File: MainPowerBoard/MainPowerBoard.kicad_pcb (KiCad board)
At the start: 2 copper layers, 177.8 x 177.8 mm, 243 parts, among them J101 CONN_01X04, J102 CONN_01X04, J103 CONN_01X04, J104 CONN_01X02, J105 CONN_01X02, J106 CONN_01X04, J107 CONN_01X06, J108 CONN_01X04, J109 CONN_01X04, J110 CONN_01X02, J111 CONN_01X02, J112 CONN_01X02, J113 CONN_01X02, J114 CONN_01X02, J115 CONN_01X02, J116 CONN_01X02, J117 CONN_01X02, J118 CONN_01X02, J119 CONN_01X02, J120 CONN_01X02, J121 CONN_01X02, J122 CONN_01X02, J123 CONN_01X02, J124 CONN_01X02, J125 CONN_01X02, J126 CONN_01X02, J127 CONN_01X02, J128 CONN_01X02, J129 CONN_01X02, J130 MOUNTING_HOLE, J131 MOUNTING_HOLE, J132 MOUNTING_HOLE, J133 MOUNTING_HOLE, SW701 GPTS203211B, U1001 LMR16030S, U1101 LMR16030S, U1201 LMR16030S, U1301 LMR16030S, U1401 LMR16030S, U201 LMR16030S, U301 LMR16030S, U701 ZXTR2012Z-7, U702 TLV271IDBVR, U703 LTC2950-1, U704 TLC393, U801 LMR16030S, U901 LMR16030S

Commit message: Done with layout - ready for final review before fab.
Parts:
- added G***: LOGO, hyperCustom:ParadigmLogo, F.Cu at (88.9, 88.9)
- D1004, D1104, D1204, D1304, D1404, D204, D804, D904: value 30V -> 28V
- D303: value 6V -> 7.5V
- D402, D502, D602: footprint Diodes_SMD:SOD-123 -> hyperCustom:SOD-123
- D501: footprint DD-PAK_TO263_SingleDiode_ThermalVias -> hyperCustom:DD-PAK_TO263_SingleDiode_ThermalVias
- J101, J102, J103, J106, J108, J109: footprint hyperCustom:CONN_PHOENIX_1844236_4PIN -> hyperCustom:CONN_PHOENIX_1844236_4PIN_1
- R1004, R1104, R1204, R1304, R1404, R204, R804, R904: value R -> 400
- R304: value R -> 300; footprint Resistors_SMD:R_1206_HandSoldering -> SMD_Packages:SMD-1206_Pol
- R401, R501, R601: value R -> 1.5k
- R703: value 10k -> 500k
- R705, R709: value R -> 300
- U701: value ZXTR2012Z-7 -> UA78L05CPK
- moved D403 5.78 mm to (20.8, 116.1), turned to 180 degrees
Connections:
- C702 pad 1: /On-Off Switch/12V0 -> /On-Off Switch/5V0
- D701 pad 2: /On-Off Switch/12V0 -> /On-Off Switch/5V0
- D702 pad 2: /On-Off Switch/12V0 -> /On-Off Switch/5V0
- R702 pad 1: /On-Off Switch/BBB_KILL_12V -> /On-Off Switch/BBB_KILL_5V
- R703 pad 1: /On-Off Switch/12V0 -> /On-Off Switch/5V0
- R704 pad 1: /On-Off Switch/12V0 -> /On-Off Switch/5V0
- R706 pad 1: /On-Off Switch/12V0 -> /On-Off Switch/5V0
- R707 pad 1: /On-Off Switch/12V0 -> /On-Off Switch/5V0
- U701 pad VO: /On-Off Switch/12V0 -> /On-Off Switch/5V0
- U702 pad 1: /On-Off Switch/BBB_KILL_12V -> /On-Off Switch/BBB_KILL_5V
- U702 pad 5: /On-Off Switch/12V0 -> /On-Off Switch/5V0
- U703 pad 1: /On-Off Switch/12V0 -> /On-Off Switch/5V0
- U703 pad 8: /On-Off Switch/BBB_KILL_12V -> (no net)
- U704 pad 8: /On-Off Switch/12V0 -> (no net)
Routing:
- net /On-Off Switch/5V0: track 0.00 -> 90.0 mm
- net /On-Off Switch/12V0: track 90.0 -> 0.00 mm
- net /On-Off Switch/BBB_KILL_5V: track 0.00 -> 55.4 mm, vias 0 -> 6
- net /On-Off Switch/BBB_KILL_12V: track 55.4 -> 0.00 mm, vias 6 -> 0
- net (no net): track 0.00 -> 0.90 mm
- net GND: track 610.3 -> 609.4 mm
- net Net-(D402-Pad2): track 2.15 -> 3.02 mm
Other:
- net class Power: clearance 0.2 -> 0
- net class VBATT added: clearance 0.84, trace_width 0.25, via_dia 0.8, via_drill 0.4
- board text added: "+"
- board text added: "-"
- board text added: "ALL CONN THIS SIDE 24V REG 1.5A, 3A MAX PER BLOCK"
- board text added: "J101-103 BATT CONN 1: VBAT<42V 2: GND 3: AUX48V 4: AUXGND"
- board text added: "J104 AUX 48V (OUT) TO EBATT"
- board text added: "J105 AUX 48V (IN)"
- board text added: "J106 EBAT CONN 1: VBAT 2: STATE 3-4: GND"
- board text added: "J107 LED CONN 1: STATE 2: VBAT 3: PB 4-6: GND"
- board text added: "J108 BBB CONN 1-2: KILL 3: INT 4: GND"
- board text added: "J109: 5V REG 1-2: 5V, 3-4: GND 1.5A, 3A MAX"
- board text added: "J127-129: 24V REG 1.5A, 3A MAX (COMB.)"

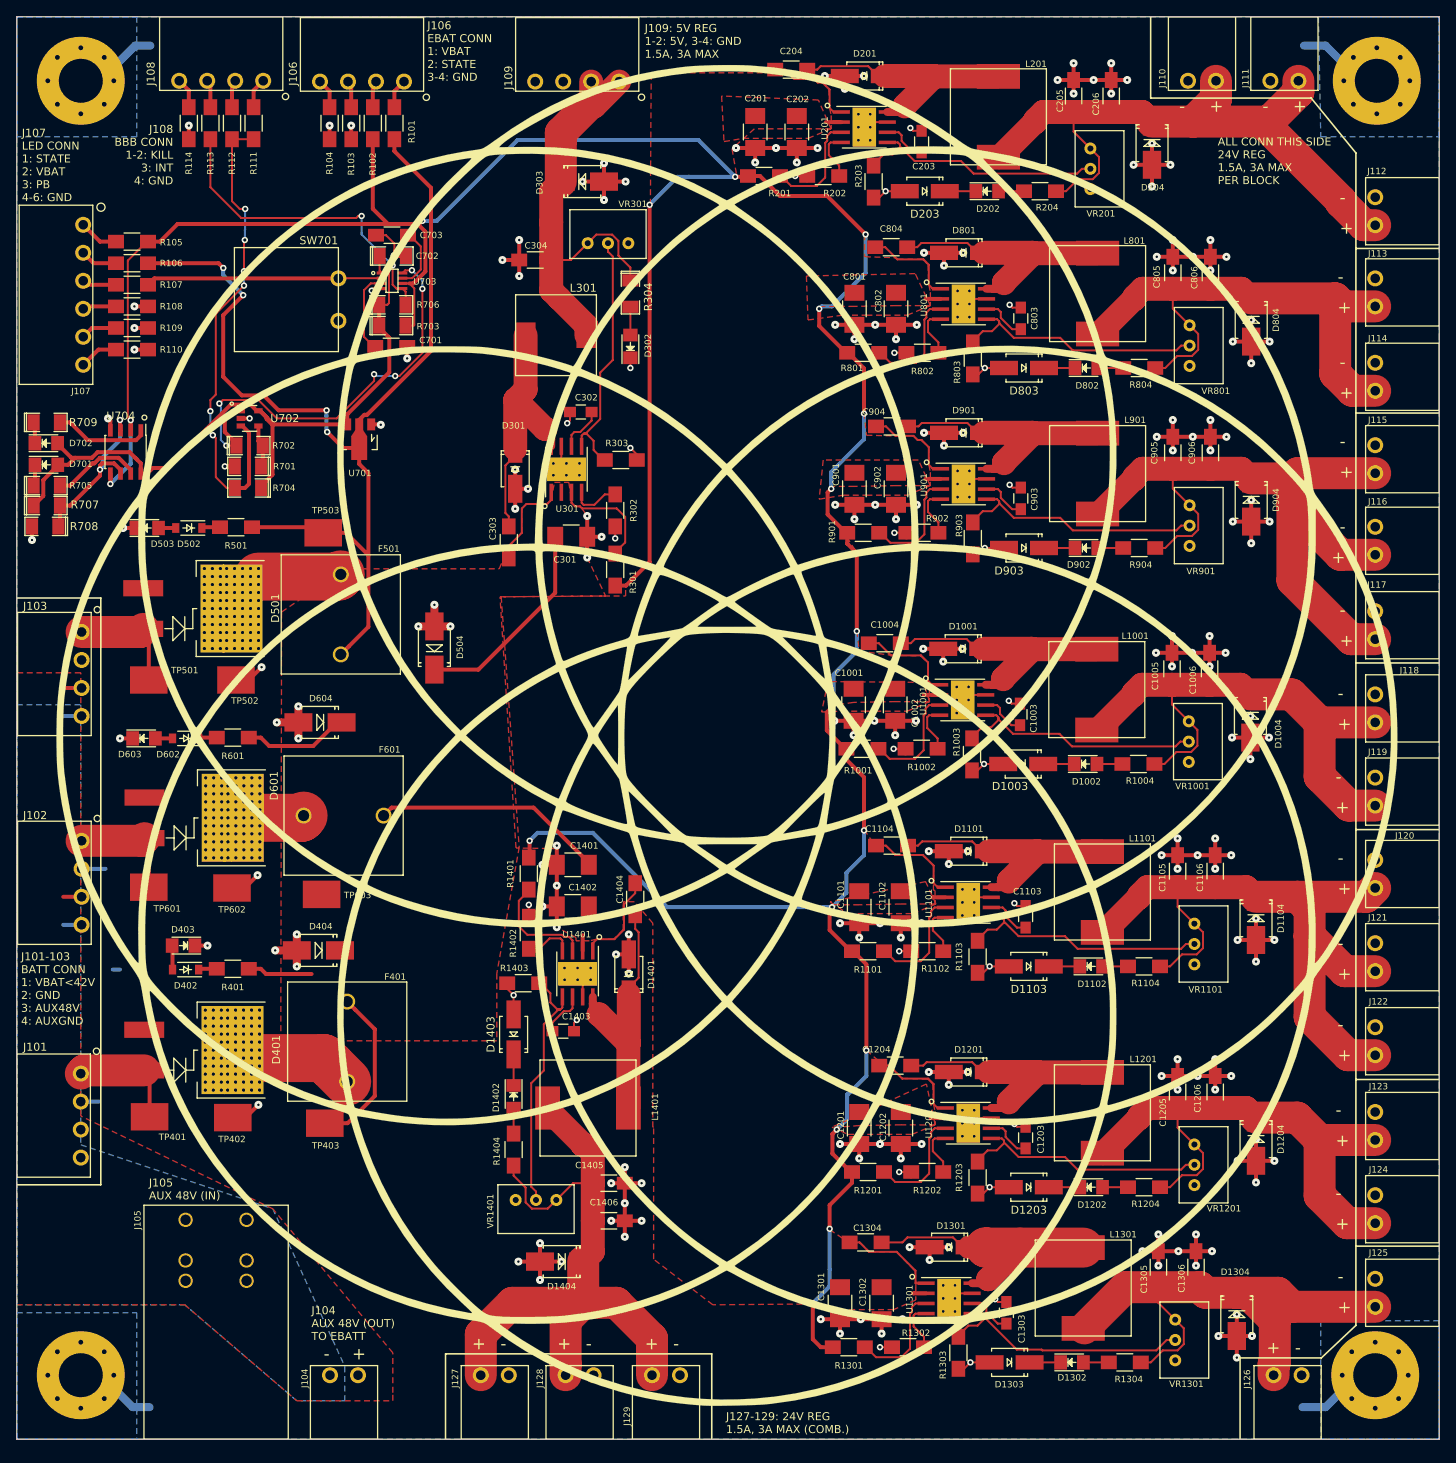
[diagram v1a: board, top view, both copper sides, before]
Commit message: Archived Rev_001 MainPowerBoard. Updated layout for pending Rev_002 release. Updated schematic components where necessary.
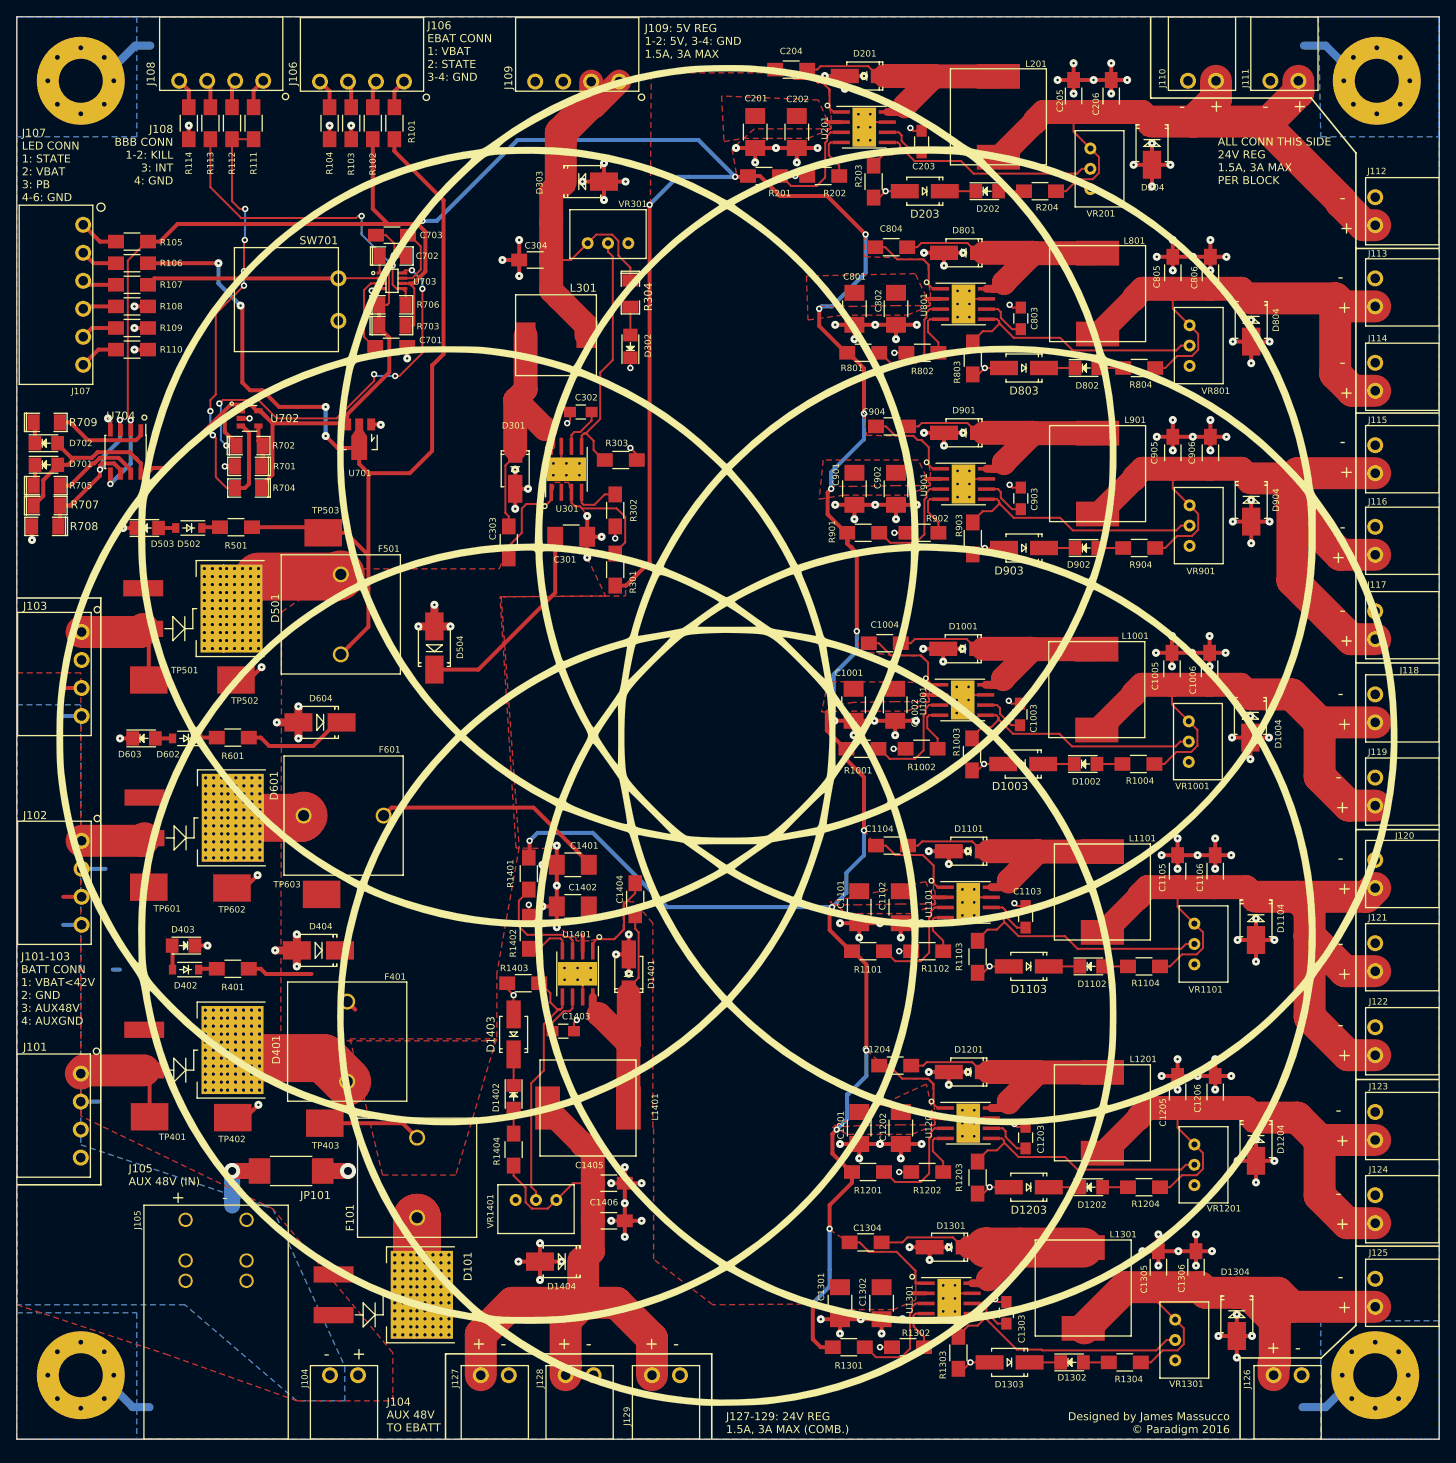
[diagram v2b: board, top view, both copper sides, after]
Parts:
- added D101: VB30100S-E3/8W, hyperCustom:DD-PAK_TO263_SingleDiode_ThermalVias, F.Cu at (54.7, 154.1)
- added F101: 0031.3804, hyperCustom:SCHURTER_0031_3804_FUSE, F.Cu at (57.5, 152.6)
- added G***: LOGO, hyperCustom:ParadigmLogoRelief, F.Cu at (88.9, 88.9)
- added JP101: JUMPER, Resistors_SMD:R_2512_HandSoldering, F.Cu at (34.3, 144.3)
- D404, D504, D604: value 60V -> 56V
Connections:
- R703 pad 1: /On-Off Switch/5V0 -> /STATE
- R703 pad 2: /STATE -> /On-Off Switch/5V0
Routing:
- net /On-Off Switch/5V0: track 90.0 -> 76.0 mm
- net /STATE: track 436.3 -> 449.1 mm
- net /GND_FROM_LINE: track 4.50 -> 12.2 mm, vias 0 -> 1
- net Net-(D101-Pad2): track 0.00 -> 5.64 mm
- net GND: track 609.4 -> 612.6 mm, vias 222 -> 223
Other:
- net class VBATT: clearance 0.84 -> 0.6
- board text added: "Designed by James Massucco © Paradigm 2016"
- board text added: "J104 AUX 48V TO EBATT"
- board text removed: "J104 AUX 48V (OUT) TO EBATT"

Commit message: Finished schematic/layout for MainPowerBoard Rev 2
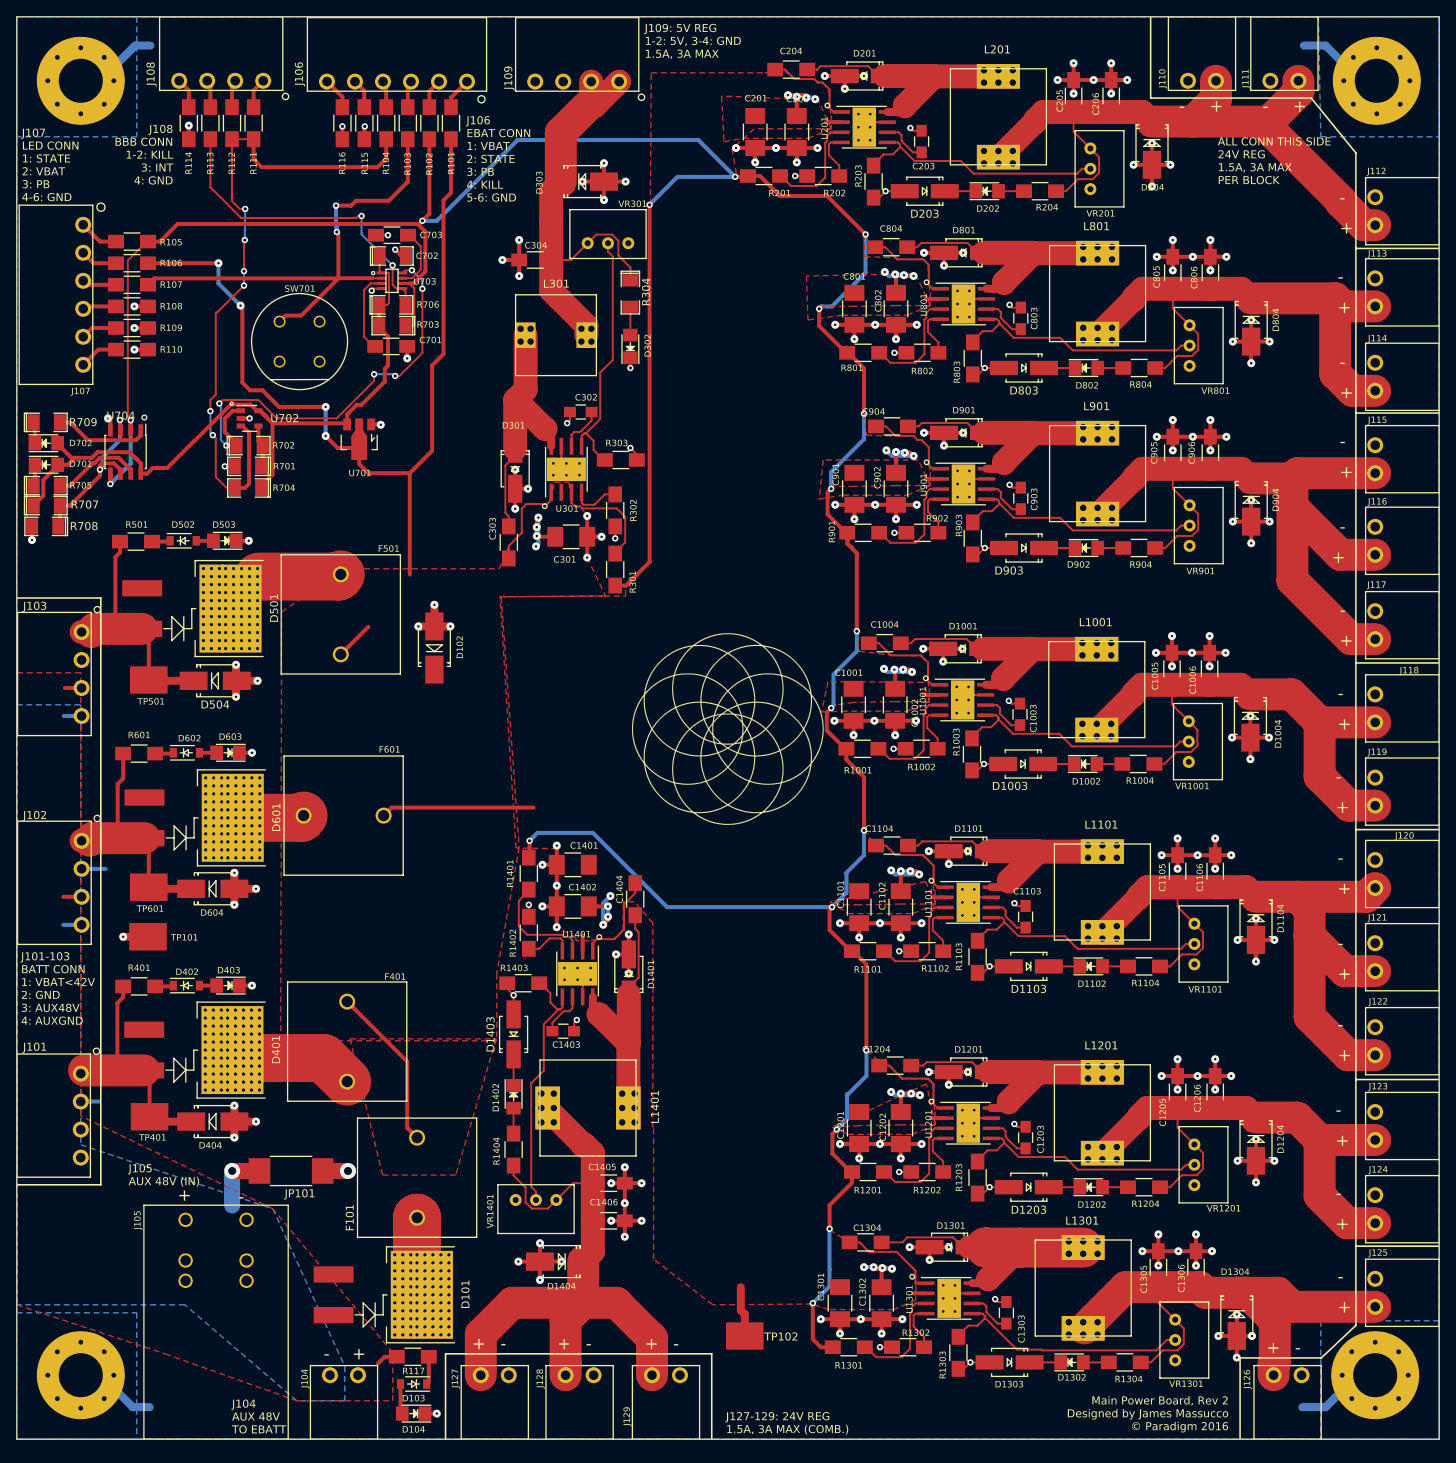
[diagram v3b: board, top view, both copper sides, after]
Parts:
- removed the G*** at (88.9, 88.9)
- removed TP402, TP403, TP502, TP503, TP602, TP603: Testpoint, hyperCustom:TP_SMT_Keystone
- added D103: 25V, hyperCustom:SOD-123, F.Cu at (49.6, 170.9)
- added D104: GREEN, LEDs:LED_1206, F.Cu at (49.6, 174.6)
- added D504: 56V, Diodes_SMD:SMB_Handsoldering, F.Cu at (24.8, 83.0)
- added G***: LOGO, hyperCustom:ParadigmLogo_1x1, F.Cu at (88.9, 88.9)
- added R115: 0, Resistors_SMD:R_1206_HandSoldering, F.Cu at (43.4, 13.3)
- added R116: 0, Resistors_SMD:R_1206_HandSoldering, F.Cu at (40.7, 13.3)
- added R117: 1.5k, Resistors_SMD:R_1206_HandSoldering, F.Cu at (49.5, 167.5)
- added TP101: Testpoint, hyperCustom:TP_SMT_Keystone, F.Cu at (16.4, 115.0)
- added TP102: Testpoint, hyperCustom:TP_SMT_Keystone, F.Cu at (91.0, 164.9)
- J106: value CONN_01X04 -> CONN_01X06; footprint hyperCustom:CONN_PHOENIX_1844236_4PIN_1 -> CONN_PHOENIX_1844252_6PIN
- L1001, L1101, L1201, L1301, L1401, L201, L801, L901: footprint hyperCustom:47uIND_CDRH127_LDNP-470MC_SUMIDA -> hyperCustom:47uIND_CDRH127_LDNP-470MC_SUMIDA_heatsink
- L301: footprint hyperCustom:15uIND_SLF10165T-150M3R13PF_BOURNS -> hyperCustom:15uIND_SLF10165T-150M3R13PF_BOURNS_heatsink
- SW701: value GPTS203211B -> KS-01Q-01; footprint hyperCustom:PBSW_CW_GPTS203211B -> hyperCustom:SW_Eswitch_KS-01Q-01
- U701: value UA78L05CPK -> AP2204RA-5.0TRG1
- moved D404 25.1 mm to (24.5, 138.1), turned to 0 degrees
- moved D604 24.7 mm to (24.5, 109.0), turned to 0 degrees
- moved R501 12.6 mm to (14.9, 65.6), turned to 0 degrees
- moved R401 11.9 mm to (15.3, 121.2), turned to 0 degrees
- moved R601 11.9 mm to (15.3, 92.1), turned to 0 degrees
- moved D603 10.7 mm to (26.4, 92.0), turned to 180 degrees
- moved D503 9.83 mm to (26.0, 65.5), turned to 180 degrees
- moved J106 7.87 mm to (58.7, 0.10)
- moved D403 7.48 mm to (26.4, 121.1)
- moved R103 7.07 mm to (48.9, 13.3)
- moved R101 7.07 mm to (54.3, 13.3)
- moved R102 7.07 mm to (51.6, 13.3)
- moved R104 7.07 mm to (46.2, 13.3)
- moved SW701 6.78 mm to (32.8, 38.1)
- moved D402 2.00 mm to (21.2, 121.1), turned to 0 degrees
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- renumbered D504 to D102
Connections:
- D404 pad 1: /VCC_BATT_COMB -> /VCC_BATT1
- D604 pad 1: /VCC_BATT_COMB -> /VCC_BATT2
- R103 pad 1: GND -> /SW_HI
- R104 pad 1: GND -> /BBB_ONOFF
- R401 pad 1: /VCC_BATT_COMB -> /VCC_BATT1
- R501 pad 1: /VCC_BATT_COMB -> /VCC_BATT3
- R601 pad 1: /VCC_BATT_COMB -> /VCC_BATT2
- U703 pad 8: (no net) -> /On-Off Switch/BBB_KILL_5V
- U704 pad 8: (no net) -> /On-Off Switch/5V0
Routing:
- net /SW_HI: track 29.5 -> 63.9 mm, vias 0 -> 2
- net /BBB_ONOFF: track 60.9 -> 83.3 mm
- net /VCC_BATT3: track 14.5 -> 33.5 mm
- net /VCC_BATT1: track 14.2 -> 32.7 mm
- net /VCC_BATT2: track 14.4 -> 32.8 mm
- net /STATE: track 449.1 -> 435.5 mm
- net /On-Off Switch/5V0: track 76.0 -> 89.0 mm
- net /VCC_BATT_COMB: track 250.6 -> 258.8 mm, vias 4 -> 40
- net Net-(J106-Pad6): track 0.00 -> 4.00 mm
- net Net-(D103-Pad2): track 0.00 -> 3.79 mm
- net Net-(J106-Pad5): track 0.00 -> 3.68 mm
- net Net-(D103-Pad1): track 0.00 -> 3.51 mm
- net GND: track 612.6 -> 609.5 mm, vias 223 -> 226
- net /48V0_FROM_LINE: track 4.40 -> 7.17 mm
- net (no net): track 0.90 -> 0.00 mm
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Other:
- board text added: "J106 EBAT CONN 1: VBAT 2: STATE 3: PB 4: KILL 5-6: GND"
- board text added: "Main Power Board, Rev 2 Designed by James Massucco © Paradigm 2016"
- board text removed: "Designed by James Massucco © Paradigm 2016"
- board text removed: "J106 EBAT CONN 1: VBAT 2: STATE 3-4: GND"
